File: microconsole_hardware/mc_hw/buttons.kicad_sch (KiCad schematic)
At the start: 33 parts, among them SW10 TL3301NF160QG, SW11 TL3301NF160QG, SW12 TL3301NF160QG, SW13 TL3301NF160QG, SW14 TL3301NF160QG, SW15 TL3301NF160QG, SW16 Joystick, SW17 Joystick, SW2 TL3301NF160QG, SW3 TL3301NF160QG, SW4 TL3301NF160QG, SW5 TL3301NF160QG, SW6 TL3301NF160QG, SW7 TL3301NF160QG, SW8 TL3301NF160QG, SW9 TL3301NF160QG, U3 MCP23017-E/SO, U4 ADS7828E/2K5

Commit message: fix capacitors
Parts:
- removed C9: 1uF, Capacitor_SMD:C_0805_2012Metric, symbol PCM_SparkFun-Capacitor:2.2uF_0805_25V_20%
- added C9: 1uF, Capacitor_SMD:C_0805_2012Metric, symbol Device:C
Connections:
- net 3v3_ADC: now also C9.1
- net GND: now also C9.2
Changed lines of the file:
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@@
 	(wire
 		(pts
+			(xy 207.01 52.07) (xy 207.01 50.8)
+		)
+		(stroke
+			(width 0)
+			(type default)
+		)
+	)
+	(wire
+		(pts
 			(xy 195.58 43.18) (xy 193.04 43.18)
 		)
@@
 	(wire
 		(pts
-			(xy 207.01 49.53) (xy 207.01 48.26)
-		)
-		(stroke
-			(width 0)
-			(type default)
-		)
-	)
-	(wire
-		(pts
 			(xy 240.03 41.91) (xy 240.03 39.37)
 		)
@@
 	(global_label "GND"
 		(shape input)
-		(at 207.01 49.53 270)
+		(at 207.01 52.07 270)
 		(fields_autoplaced yes)
 		(effects
@@
 		)
 		(property "Intersheetrefs" "${INTERSHEET_REFS}"
-			(at 207.01 56.3857 90)
+			(at 207.01 58.9257 90)
 			(hide yes)
 			(show_name no)
@@
 	)
 	(symbol
-		(lib_id "PCM_SparkFun-Capacitor:2.2uF_0805_25V_20%")
-		(at 207.01 45.72 0)
-		(unit 1)
-		(body_style 1)
-		(exclude_from_sim no)
-		(in_bom yes)
-		(on_board yes)
-		(in_pos_files yes)
-		(dnp no)
-		(property "Reference" "C9"
-			(at 209.042 45.466 0)
-			(show_name no)
-			(do_not_autoplace no)
-			(effects
-				(font
-					(size 1.27 1.27)
-				)
-				(justify left)
-			)
-		)
-		(property "Value" "1uF"
-			(at 208.788 47.244 0)
-			(show_name no)
-			(do_not_autoplace no)
-			(effects
-				(font
-					(size 1.27 1.27)
-				)
-				(justify left)
-			)
-		)
-		(property "Footprint" "Capacitor_SMD:C_0805_2012Metric"
-			(at 207.01 57.15 0)
-			(hide yes)
-			(show_name no)
-			(do_not_autoplace no)
-			(effects
-				(font
-					(size 1.27 1.27)
-				)
-			)
-		)
-		(property "Datasheet" "https://cdn.sparkfun.com/assets/8/a/4/a/5/Kemet_Capacitor_Datasheet.pdf"
-			(at 208.28 62.23 0)
-			(hide yes)
-			(show_name no)
-			(do_not_autoplace no)
-			(effects
-				(font
-					(size 1.27 1.27)
-				)
-			)
-		)
-		(property "Description" "Unpolarized capacitor"
-			(at 207.01 64.77 0)
-			(hide yes)
-			(show_name no)
-			(do_not_autoplace no)
-			(effects
-				(font
-					(size 1.27 1.27)
-				)
-			)
-		)
-		(property "PROD_ID" "CAP-11624"
-			(at 205.74 59.69 0)
-			(hide yes)
-			(show_name no)
-			(do_not_autoplace no)
-			(effects
-				(font
-					(size 1.27 1.27)
-				)
-			)
-		)
-		(property "Voltage" "25V"
-			(at 215.138 45.212 0)
-			(show_name no)
-			(do_not_autoplace no)
-			(effects
-				(font
-					(size 1.27 1.27)
-				)
-			)
-		)
-		(property "Tolerance" "20%"
-			(at 215.138 47.752 0)
-			(show_name no)
-			(do_not_autoplace no)
-			(effects
-				(font
-					(size 1.27 1.27)
-				)
-			)
-		)
-		(pin "2"
-		)
-		(pin "1"
-		)
-		(instances
-			(project "top"
-				(path "/3433afdc-e53a-48bd-a2b1-9fdee73e8b40/adf9b4c7-5a8e-47d3-8a4f-7ca4793a2375"
-					(reference "C9")
-					(unit 1)
-				)
-			)
-			(project "mc_hw"
-				(path "/719302af-dc57-4543-bdcd-0eb891c4def3"
-					(reference "C9")
-					(unit 1)
-				)
-			)
-		)
-	)
-	(symbol
 		(lib_id "project_parts:C0805C104K5RAC7210")
 		(at 143.51 85.09 0)
@@
 					(unit 1)
 				)
+			)
+		)
+	)
+	(symbol
+		(lib_id "Device:C")
+		(at 207.01 46.99 0)
+		(unit 1)
+		(body_style 1)
+		(exclude_from_sim no)
+		(in_bom yes)
+		(on_board yes)
+		(in_pos_files yes)
+		(dnp no)
+		(property "Reference" "C9"
+			(at 209.042 46.736 0)
+			(show_name no)
+			(do_not_autoplace no)
+			(effects
+				(font
+					(size 1.27 1.27)
+				)
+				(justify left)
+			)
+		)
+		(property "Value" "1uF"
+			(at 208.788 48.514 0)
+			(show_name no)
+			(do_not_autoplace no)
+			(effects
+				(font
+					(size 1.27 1.27)
+				)
+				(justify left)
+			)
+		)
+		(property "Footprint" "Capacitor_SMD:C_0805_2012Metric"
+			(at 207.9752 50.8 0)
+			(hide yes)
+			(show_name no)
+			(do_not_autoplace no)
+			(effects
+				(font
+					(size 1.27 1.27)
+				)
+			)
+		)
+		(property "Datasheet" "https://cdn.sparkfun.com/assets/8/a/4/a/5/Kemet_Capacitor_Datasheet.pdf"
+			(at 207.01 46.99 0)
+			(hide yes)
+			(show_name no)
+			(do_not_autoplace no)
+			(effects
+				(font
+					(size 1.27 1.27)
+				)
+			)
+		)
+		(property "Description" "Unpolarized capacitor"
+			(at 207.01 46.99 0)
+			(hide yes)
+			(show_name no)
+			(do_not_autoplace no)
+			(effects
+				(font
+					(size 1.27 1.27)
+				)
+			)
+		)
+		(property "PROD_ID" "CAP-11624"
+			(at 205.74 60.96 0)
+			(hide yes)
+			(show_name no)
+			(do_not_autoplace no)
+			(effects
+				(font
+					(size 1.27 1.27)
+				)
+			)
+		)
+		(property "Voltage" "25V"
+			(at 215.138 46.482 0)
+			(show_name no)
+			(do_not_autoplace no)
+			(effects
+				(font
+					(size 1.27 1.27)
+				)
+			)
+		)
+		(property "Tolerance" "20%"
+			(at 215.138 49.022 0)
+			(show_name no)
+			(do_not_autoplace no)
+			(effects
+				(font
+					(size 1.27 1.27)
+				)
+			)
+		)
+		(pin "2"
+		)
+		(pin "1"
+		)
+		(instances
+			(project "top"
+				(path "/3433afdc-e53a-48bd-a2b1-9fdee73e8b40/adf9b4c7-5a8e-47d3-8a4f-7ca4793a2375"
+					(reference "C9")
+					(unit 1)
+				)

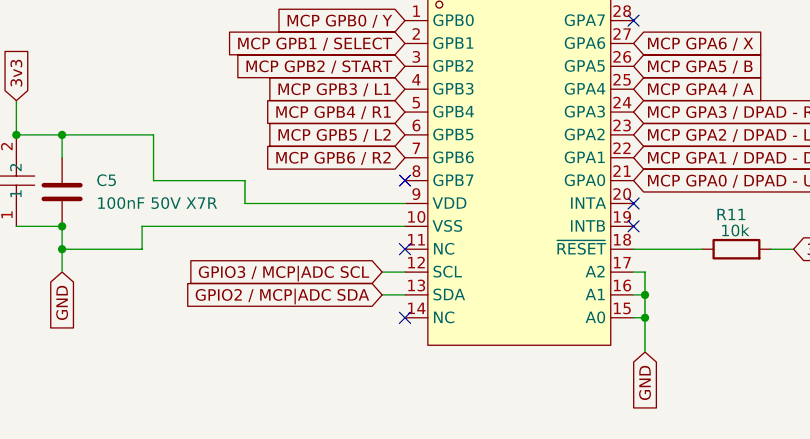
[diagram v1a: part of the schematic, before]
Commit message: cleanup ic symbol pin types
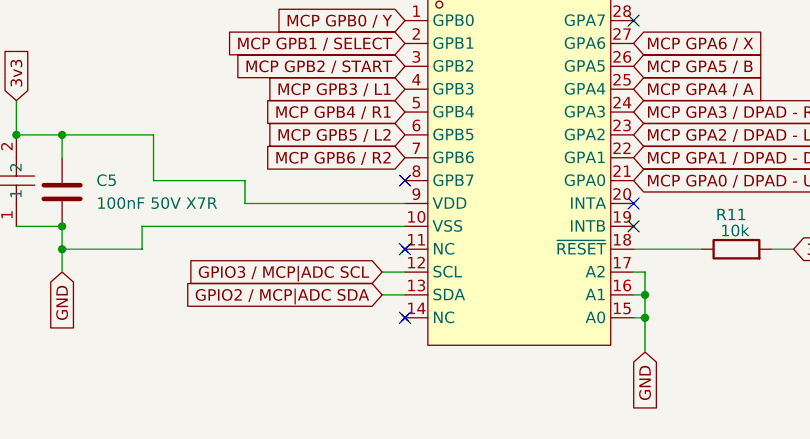
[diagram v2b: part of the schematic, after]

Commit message: consolidate parts 1
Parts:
- R11: MPN (none) -> RC0603FR-0710KL; Manufacturer (none) -> YAGEO; Power (none) -> 0.1W; Tolerance (none) -> 1%
- R12, R13, R14, R15: MPN (none) -> RC0603FR-071KL; Manufacturer (none) -> YAGEO; Power (none) -> 0.1W; Tolerance (none) -> 1%

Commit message: second fix
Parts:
- FB1: MPN (none) -> MPZ1608S601ATA00; Manufacturer (none) -> TDK
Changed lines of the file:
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@@
+			)
+		)
+		(property "MPN" "MPZ1608S601ATA00"
+			(at 264.16 52.07 90)
+			(hide yes)
+			(show_name no)
+			(do_not_autoplace no)
+			(effects
+				(font
+					(size 1.27 1.27)
+				)
+			)
+		)
+		(property "Manufacturer" "TDK"
+			(at 264.16 52.07 90)
+			(hide yes)
+			(show_name no)
+			(do_not_autoplace no)
+			(effects
+				(font
+					(size 1.27 1.27)
+				)
 			)
 		)

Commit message: fix up bom
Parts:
- C9: MPN (none) -> GRM21BR71C105KA01L; Manufacturer (none) -> Murata Electronics
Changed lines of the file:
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@@
 			)
 		)
-		(property "Datasheet" "https://cdn.sparkfun.com/assets/8/a/4/a/5/Kemet_Capacitor_Datasheet.pdf"
+		(property "Datasheet" ""
 			(at 207.01 46.99 0)
 			(hide yes)
@@
 			(at 207.01 46.99 0)
 			(hide yes)
+			(show_name no)
+			(do_not_autoplace no)
+			(effects
+				(font
+					(size 1.27 1.27)
+				)
+			)
+		)
+		(property "MPN" "GRM21BR71C105KA01L"
+			(at 207.01 46.99 0)
+			(hide yes)
+			(show_name no)
+			(do_not_autoplace no)
+			(effects
+				(font
+					(size 1.27 1.27)
+				)
+			)
+		)
+		(property "Manufacturer" "Murata Electronics"
+			(at 207.01 46.99 0)
+			(hide yes)

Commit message: bom cleanup
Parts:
- C10, C11, C12, C5, C7, C8: Tolerance (none) -> 10%; Voltage (none) -> 50V
- C13, C4: Tolerance (none) -> 10%; Voltage (none) -> 10V
- C9: PROD_ID CAP-11624 -> (none); Tolerance 20% -> 10%; Voltage 25V -> 16V
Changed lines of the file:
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@@
 			)
 		)
+		(property "Tolerance" "10%"
+			(at 143.51 85.09 0)
+			(hide yes)
+			(show_name no)
+			(do_not_autoplace no)
+			(effects
+				(font
+					(size 1.27 1.27)
+				)
+			)
+		)
+		(property "Voltage" "50V"
+			(at 143.51 85.09 0)
+			(hide yes)
+			(show_name no)
+			(do_not_autoplace no)
+			(effects
+				(font
+					(size 1.27 1.27)
+				)
+			)
+		)
 		(pin "1"
 		)
@@
 			)
 		)
+		(property "Tolerance" "10%"
+			(at 229.87 31.75 0)
+			(hide yes)
+			(show_name no)
+			(do_not_autoplace no)
+			(effects
+				(font
+					(size 1.27 1.27)
+				)
+			)
+		)
+		(property "Voltage" "50V"
+			(at 229.87 31.75 0)
+			(hide yes)
+			(show_name no)
+			(do_not_autoplace no)
+			(effects
+				(font
+					(size 1.27 1.27)
+				)
+			)
+		)
 		(pin "1"
 		)
@@
 			)
 		)
-		(property "Datasheet" "https://lcsc.com/product-detail/presales_AVX-1206ZD106KAT2A_C597553.html"
+		(property "Datasheet" ""
 			(at 259.08 31.75 0)
 			(hide yes)
@@
 			)
 		)
+		(property "Tolerance" "10%"
+			(at 248.92 31.75 90)
+			(hide yes)
+			(show_name no)
+			(do_not_autoplace no)
+			(effects
+				(font
+					(size 1.27 1.27)
+				)
+			)
+		)
+		(property "Voltage" "10V"
+			(at 248.92 31.75 90)
+			(hide yes)
+			(show_name no)
+			(do_not_autoplace no)
+			(effects
+				(font
+					(size 1.27 1.27)
+				)
+			)
+		)
 		(pin "1"
 		)
@@
 			)
 		)
-		(property "Datasheet" "https://lcsc.com/product-detail/presales_AVX-1206ZD106KAT2A_C597553.html"
+		(property "Datasheet" ""
 			(at 72.39 165.1 0)
 			(hide yes)
@@
 			)
 		)
+		(property "Tolerance" "10%"
+			(at 62.23 165.1 90)
+			(hide yes)
+			(show_name no)
+			(do_not_autoplace no)
+			(effects
+				(font
+					(size 1.27 1.27)
+				)
+			)
+		)
+		(property "Voltage" "10V"
+			(at 62.23 165.1 90)
+			(hide yes)
+			(show_name no)
+			(do_not_autoplace no)
+			(effects
+				(font
+					(size 1.27 1.27)
+				)
+			)
+		)
 		(pin "1"
 		)
@@
 			)
 		)
-		(property "PROD_ID" "CAP-11624"
+		(property "PROD_ID" ""
 			(at 205.74 60.96 0)
 			(hide yes)
@@
 			)
 		)
-		(property "Voltage" "25V"
+		(property "Voltage" "16V"
 			(at 215.138 46.482 0)
 			(show_name no)
@@
 			)
 		)
-		(property "Tolerance" "20%"
+		(property "Tolerance" "10%"
 			(at 215.138 49.022 0)
 			(show_name no)
@@
 			)
 		)
+		(property "Tolerance" "10%"
+			(at 143.51 67.31 0)
+			(hide yes)
+			(show_name no)
+			(do_not_autoplace no)
+			(effects
+				(font
+					(size 1.27 1.27)
+				)
+			)
+		)
+		(property "Voltage" "50V"
+			(at 143.51 67.31 0)
+			(hide yes)
+			(show_name no)
+			(do_not_autoplace no)
+			(effects
+				(font
+					(size 1.27 1.27)
+				)
+			)
+		)
 		(pin "1"
 		)
@@
 			)
 		)
+		(property "Tolerance" "10%"
+			(at 240.03 86.36 0)
+			(hide yes)
+			(show_name no)
+			(do_not_autoplace no)
+			(effects
+				(font
+					(size 1.27 1.27)
+				)
+			)
+		)
+		(property "Voltage" "50V"
+			(at 240.03 86.36 0)
+			(hide yes)
+			(show_name no)
+			(do_not_autoplace no)
+			(effects
+				(font
+					(size 1.27 1.27)
+				)
+			)
+		)
 		(pin "1"
 		)
@@
 			)
 		)
+		(property "Tolerance" "10%"
+			(at 67.31 166.37 0)
+			(hide yes)
+			(show_name no)
+			(do_not_autoplace no)
+			(effects
+				(font
+					(size 1.27 1.27)
+				)
+			)
+		)
+		(property "Voltage" "50V"
+			(at 67.31 166.37 0)
+			(hide yes)
+			(show_name no)
+			(do_not_autoplace no)
+			(effects
+				(font
+					(size 1.27 1.27)
+				)
+			)
+		)
 		(pin "1"
 		)
@@
 			(at 240.03 67.31 0)
 			(hide yes)
+			(show_name no)
+			(do_not_autoplace no)
+			(effects
+				(font
+					(size 1.27 1.27)
+				)
+			)
+		)
+		(property "Tolerance" "10%"
+			(at 240.03 67.31 0)
+			(hide yes)
+			(show_name no)
+			(do_not_autoplace no)
+			(effects
+				(font
+					(size 1.27 1.27)
+				)
+			)
+		)
+		(property "Voltage" "50V"
+			(at 240.03 67.31 0)
+			(hide yes)

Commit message: bom
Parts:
- SW16, SW17: value Joystick -> FJH10K-S2; MPN (none) -> FJH10K-S2; Manufacturer (none) -> Favor Electronics / Favor Union; PROD_ID COMP-09744 -> (none)
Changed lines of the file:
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@@
 			)
 		)
-		(property "Value" "Joystick"
+		(property "Value" "FJH10K-S2"
 			(at 143.51 125.73 0)
 			(show_name no)
@@
 			)
 		)
-		(property "Datasheet" ""
+		(property "Datasheet" "https://mm.digikey.com/Volume0/opasdata/d220001/medias/docus/6530/FJH10K-S2.pdf"
 			(at 143.51 130.048 0)
 			(hide yes)
@@
 			)
 		)
-		(property "Description" "Directional Pad"
+		(property "Description" "Dual-axis Hall-effect joystick with push switch"
 			(at 143.51 132.588 0)
 			(hide yes)
@@
 			)
 		)
-		(property "PROD_ID" "COMP-09744"
+		(property "PROD_ID" ""
 			(at 143.51 127.508 0)
 			(hide yes)
@@
 		)
 		(property "Power" ""
+			(at 143.51 111.76 0)
+			(hide yes)
+			(show_name no)
+			(do_not_autoplace no)
+			(effects
+				(font
+					(size 1.27 1.27)
+				)
+			)
+		)
+		(property "MPN" "FJH10K-S2"
+			(at 143.51 111.76 0)
+			(hide yes)
+			(show_name no)
+			(do_not_autoplace no)
+			(effects
+				(font
+					(size 1.27 1.27)
+				)
+			)
+		)
+		(property "Manufacturer" "Favor Electronics / Favor Union"
 			(at 143.51 111.76 0)
 			(hide yes)
@@
 			)
 		)
-		(property "Value" "Joystick"
+		(property "Value" "FJH10K-S2"
 			(at 240.03 125.73 0)
 			(show_name no)
@@
 			)
 		)
-		(property "Datasheet" ""
+		(property "Datasheet" "https://mm.digikey.com/Volume0/opasdata/d220001/medias/docus/6530/FJH10K-S2.pdf"
 			(at 240.03 130.048 0)
 			(hide yes)
@@
 			)
 		)
-		(property "Description" "Directional Pad"
+		(property "Description" "Dual-axis Hall-effect joystick with push switch"
 			(at 240.03 132.588 0)
 			(hide yes)
@@
 			)
 		)
-		(property "PROD_ID" "COMP-09744"
+		(property "PROD_ID" ""
 			(at 240.03 127.508 0)
 			(hide yes)
@@
 			(at 240.03 111.76 0)
 			(hide yes)
+			(show_name no)
+			(do_not_autoplace no)
+			(effects
+				(font
+					(size 1.27 1.27)
+				)
+			)
+		)
+		(property "MPN" "FJH10K-S2"
+			(at 240.03 111.76 0)
+			(hide yes)
+			(show_name no)
+			(do_not_autoplace no)
+			(effects
+				(font
+					(size 1.27 1.27)
+				)
+			)
+		)
+		(property "Manufacturer" "Favor Electronics / Favor Union"
+			(at 240.03 111.76 0)
+			(hide yes)

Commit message: dnp
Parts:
- SW10, SW11, SW12, SW13, SW14, SW15, SW16, SW17, SW2, SW3, SW4, SW5, SW6, SW7, SW8, SW9: now not fitted
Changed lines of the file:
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@@
 		(on_board yes)
 		(in_pos_files yes)
-		(dnp no)
+		(dnp yes)
 		(property "Reference" "SW8"
 			(at 36.83 108.712 90)
@@
 		(on_board yes)
 		(in_pos_files yes)
-		(dnp no)
+		(dnp yes)
 		(property "Reference" "SW2"
 			(at 22.86 21.082 90)
@@
 		(on_board yes)
 		(in_pos_files yes)
-		(dnp no)
+		(dnp yes)
 		(property "Reference" "SW14"
 			(at 64.77 69.342 90)
@@
 		(on_board yes)
 		(in_pos_files yes)
-		(dnp no)
+		(dnp yes)
 		(property "Reference" "SW11"
 			(at 50.8 69.342 90)
@@
 		(on_board yes)
 		(in_pos_files yes)
-		(dnp no)
+		(dnp yes)
 		(property "Reference" "SW3"
 			(at 22.86 69.342 90)
@@
 		(on_board yes)
 		(in_pos_files yes)
-		(dnp no)
+		(dnp yes)
 		(property "Reference" "SW15"
 			(at 64.77 108.458 90)
@@
 		(on_board yes)
 		(in_pos_files yes)
-		(dnp no)
+		(dnp yes)
 		(property "Reference" "SW9"
 			(at 36.83 148.082 90)
@@
 		(on_board yes)
 		(in_pos_files yes)
-		(dnp no)
+		(dnp yes)
 		(property "Reference" "SW12"
 			(at 53.34 108.712 90)
@@
 		(on_board yes)
 		(in_pos_files yes)
-		(dnp no)
+		(dnp yes)
 		(property "Reference" "SW7"
 			(at 36.83 69.342 90)
@@
 		(on_board yes)
 		(in_pos_files yes)
-		(dnp no)
+		(dnp yes)
 		(fields_autoplaced yes)
 		(property "Reference" "SW16"
@@
 		(on_board yes)
 		(in_pos_files yes)
-		(dnp no)
+		(dnp yes)
 		(property "Reference" "SW6"
 			(at 36.83 21.082 90)
@@
 		(on_board yes)
 		(in_pos_files yes)
-		(dnp no)
+		(dnp yes)
 		(property "Reference" "SW13"
 			(at 64.77 21.082 90)
@@
 		(on_board yes)
 		(in_pos_files yes)
-		(dnp no)
+		(dnp yes)
 		(property "Reference" "SW5"
 			(at 22.86 148.082 90)
@@
 		(on_board yes)
 		(in_pos_files yes)
-		(dnp no)
+		(dnp yes)
 		(fields_autoplaced yes)
 		(property "Reference" "SW17"
@@
 		(on_board yes)
 		(in_pos_files yes)
-		(dnp no)
+		(dnp yes)
 		(property "Reference" "SW4"
 			(at 22.86 108.712 90)
@@
 		(on_board yes)
 		(in_pos_files yes)
-		(dnp no)
+		(dnp yes)
 		(property "Reference" "SW10"
 			(at 50.8 21.082 90)
